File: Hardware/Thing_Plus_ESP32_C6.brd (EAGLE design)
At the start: 22.9 x 58.4 mm, 108 parts, among them J1 THING_PLUS_LOGICAL, J4 QWIIC_RIGHT_ANGLE, J5 MICRO-SDFRICTION, Q1 20V/4.2A/52mΩ/1.4W, U1 ESP32-C6-WROOM-1-NARROW, U2 RT9080-33GJ5, U3 MCP73831, U4 MAX17048

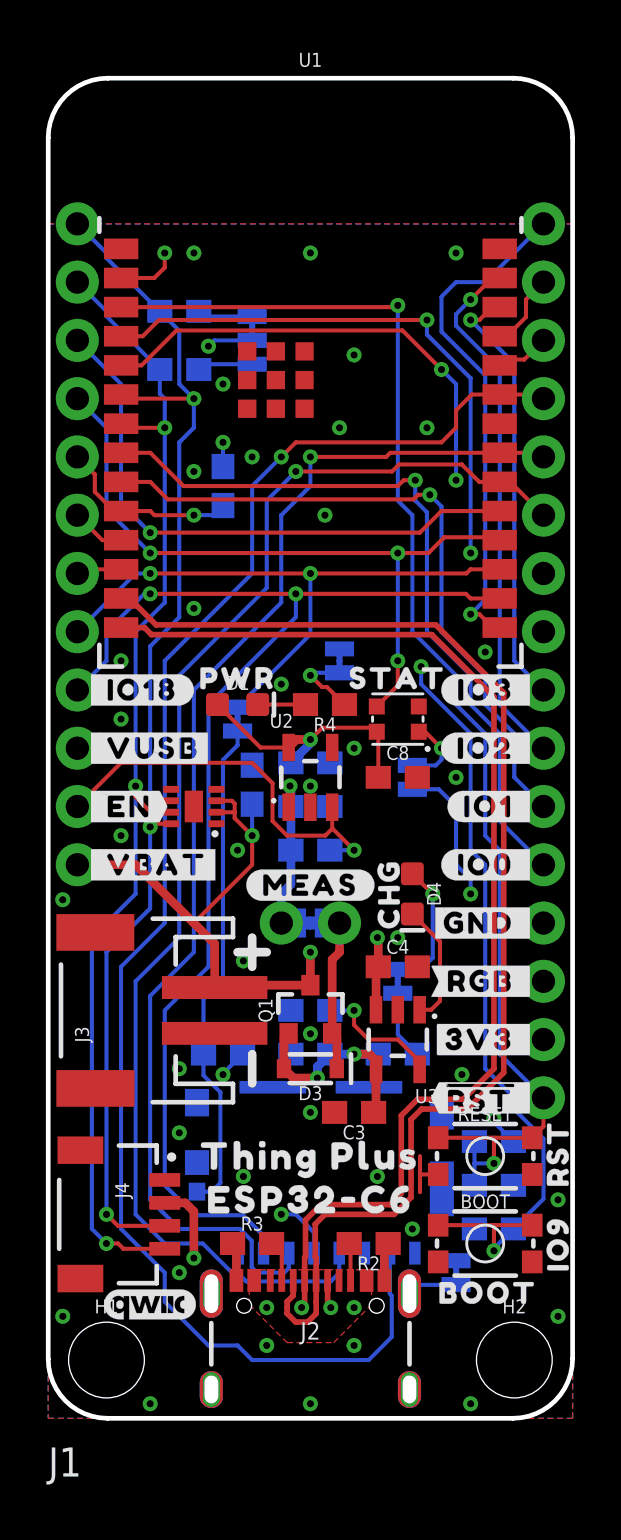
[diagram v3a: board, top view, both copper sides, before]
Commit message: Design review updates
Add fiducials
Add top mounting holes under ESP32-C6 antenna
Move OSHW logo and make bigger
Change RGB jumper to NO
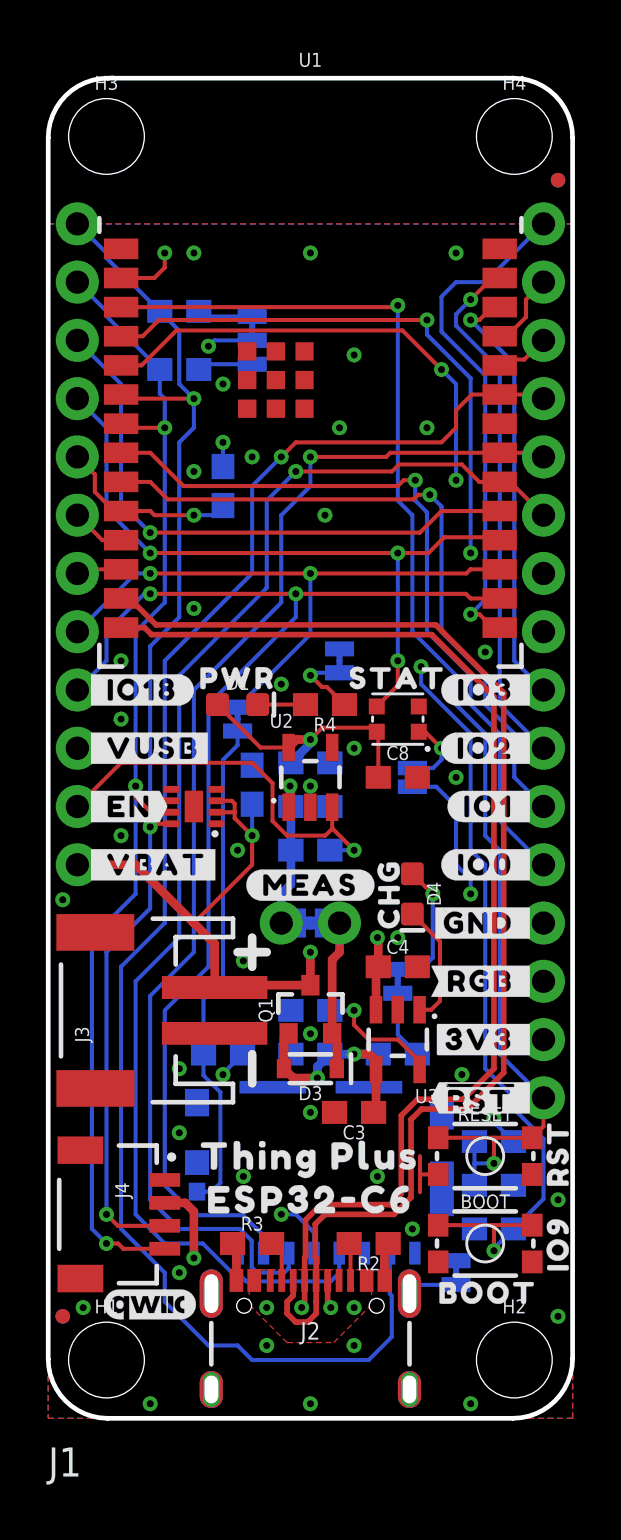
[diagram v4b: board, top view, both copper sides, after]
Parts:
- added FD1, FD2, FD3, FD4: FIDUCIALUFIDUCIAL, SparkFun-Aesthetics:FIDUCIAL-MICRO
- added H3, H4: STAND-OFF, SparkFun-Hardware:STAND-OFF
- LOGO3: value OSHW-LOGOS -> OSHW-LOGOM; device SparkFun-Aesthetics:OSHW-LOGO-S -> SparkFun-Aesthetics:OSHW-LOGO-M
- RGB: value JUMPER-SMT_2_NC_TRACE_SILK -> JUMPER-SMT_2_NO_SILK; device SparkFun-Jumpers:SMT-JUMPER_2_NC_TRACE_SILK -> SparkFun-Jumpers:SMT-JUMPER_2_NO_SILK
- moved LOGO3 20.9 mm to (5.08, 19.7)
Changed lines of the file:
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@@
 <element name="LOGO1" library="SparkFun-Aesthetics" package="SFE_LOGO_NAME_FLAME_.1" value="SFE_LOGO_NAME_FLAME.1_INCH" x="11.43" y="54.229" smashed="yes" rot="MR0"/>
 <element name="LOGO2" library="SparkFun-Aesthetics" package="QWIIC_4MM" value="QWIIC_LOGO_4MM" x="4.445" y="4.953" smashed="yes"/>
-<element name="LOGO3" library="SparkFun-Aesthetics" package="OSHW-LOGO-S" value="OSHW-LOGOS" x="10.16" y="40.005" smashed="yes" rot="MR0"/>
+<element name="LOGO3" library="SparkFun-Aesthetics" package="OSHW-LOGO-M" value="OSHW-LOGOM" x="5.08" y="19.685" smashed="yes" rot="MR0"/>
 <element name="R1" library="SparkFun-Resistors" package="0603" value="100k" x="7.62" y="40.64" smashed="yes" rot="MR90">
 <attribute name="NAME" x="8.182" y="40.64" size="0.6096" layer="26" font="vector" ratio="20" rot="MR90" align="bottom-center"/>
@@
 <element name="U$54" library="output" package="CHG0" value="" x="14.859" y="22.86" smashed="yes" rot="R90"/>
 <element name="U$55" library="output" package="STAT0" value="" x="15.24" y="32.258" smashed="yes"/>
-<element name="RGB" library="SparkFun-Jumpers" package="SMT-JUMPER_2_NC_TRACE_SILK" package3d_urn="urn:adsk.eagle:package:39281/1" value="JUMPER-SMT_2_NC_TRACE_SILK" x="15.875" y="27.94" smashed="yes" rot="MR90">
+<element name="RGB" library="SparkFun-Jumpers" package="SMT-JUMPER_2_NO_SILK" package3d_urn="urn:adsk.eagle:package:39279/1" value="JUMPER-SMT_2_NO_SILK" x="15.875" y="27.94" smashed="yes" rot="MR90">
 <attribute name="NAME" x="17.018" y="27.94" size="0.6096" layer="26" font="vector" ratio="20" rot="MR90" align="bottom-center"/>
 <attribute name="VALUE" x="14.732" y="27.94" size="0.6096" layer="28" font="vector" ratio="20" rot="MR90" align="top-center"/>
@@
 <element name="U$58" library="output" package="#RGB_#0" value="" x="21.336" y="19.05" smashed="yes"/>
 <element name="U$59" library="output" package="#_RGB#0" value="" x="21.336" y="19.05" smashed="yes" rot="MR0"/>
+<element name="H3" library="SparkFun-Hardware" package="STAND-OFF" value="STAND-OFF" x="2.54" y="55.88" smashed="yes">
+<attribute name="NAME" x="2.54" y="57.912" size="0.6096" layer="25" font="vector" ratio="20" align="bottom-center"/>
+<attribute name="VALUE" x="2.54" y="53.848" size="0.6096" layer="27" font="vector" ratio="20" align="top-center"/>
+</element>
+<element name="H4" library="SparkFun-Hardware" package="STAND-OFF" value="STAND-OFF" x="20.32" y="55.88" smashed="yes">
+<attribute name="NAME" x="20.32" y="57.912" size="0.6096" layer="25" font="vector" ratio="20" align="bottom-center"/>
+<attribute name="VALUE" x="20.32" y="53.848" size="0.6096" layer="27" font="vector" ratio="20" align="top-center"/>
+</element>
+<element name="FD1" library="SparkFun-Aesthetics" package="FIDUCIAL-MICRO" value="FIDUCIALUFIDUCIAL" x="22.225" y="53.975" smashed="yes"/>
+<element name="FD2" library="SparkFun-Aesthetics" package="FIDUCIAL-MICRO" value="FIDUCIALUFIDUCIAL" x="22.225" y="53.975" smashed="yes" rot="MR0"/>
+<element name="FD3" library="SparkFun-Aesthetics" package="FIDUCIAL-MICRO" value="FIDUCIALUFIDUCIAL" x="0.635" y="4.445" smashed="yes"/>
+<element name="FD4" library="SparkFun-Aesthetics" package="FIDUCIAL-MICRO" value="FIDUCIALUFIDUCIAL" x="0.635" y="4.445" smashed="yes" rot="MR0"/>
 </elements>
 <signals>
@@
 <via x="18.415" y="0.635" extent="1-16" drill="0.3048"/>
 <via x="4.445" y="0.635" extent="1-16" drill="0.3048"/>
-<via x="0.635" y="4.445" extent="1-16" drill="0.3048"/>
+<via x="1.524" y="4.826" extent="1-16" drill="0.3048"/>
 <via x="0.635" y="22.606" extent="1-16" drill="0.3048"/>
 <via x="8.255" y="24.765" extent="1-16" drill="0.3048"/>
@@
 <contactref element="J1" pad="26"/>
 <contactref element="RGB" pad="1"/>
-<wire x1="15.875" y1="27.4193" x2="17.0307" y2="27.4193" width="0.1778" layer="16"/>
-<wire x1="17.0307" y1="27.4193" x2="17.78" y2="26.67" width="0.1778" layer="16"/>
+<wire x1="15.875" y1="27.5336" x2="16.9164" y2="27.5336" width="0.1778" layer="16"/>
+<wire x1="16.9164" y1="27.5336" x2="17.78" y2="26.67" width="0.1778" layer="16"/>
 <wire x1="17.78" y1="26.67" x2="17.78" y2="24.13" width="0.1778" layer="16"/>
 <wire x1="17.78" y1="24.13" x2="18.415" y2="23.495" width="0.1778" layer="16"/>
@@
 <wire x1="16.425" y1="29.93" x2="17.145" y2="29.21" width="0.1778" layer="1"/>
 <via x="17.145" y="29.21" extent="1-16" drill="0.3048"/>
-<wire x1="17.145" y1="28.7147" x2="16.891" y2="28.4607" width="0.1778" layer="16"/>
-<wire x1="15.875" y1="28.4607" x2="16.891" y2="28.4607" width="0.1778" layer="16"/>
+<wire x1="17.145" y1="28.7147" x2="16.7767" y2="28.3464" width="0.1778" layer="16"/>
+<wire x1="15.875" y1="28.3464" x2="16.7767" y2="28.3464" width="0.1778" layer="16"/>
 <wire x1="17.145" y1="28.7147" x2="17.145" y2="29.21" width="0.1778" layer="16"/>
 </signal>

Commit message: Add power control to uSD card
Also add 10uF cap for uSD card
And add boot button text
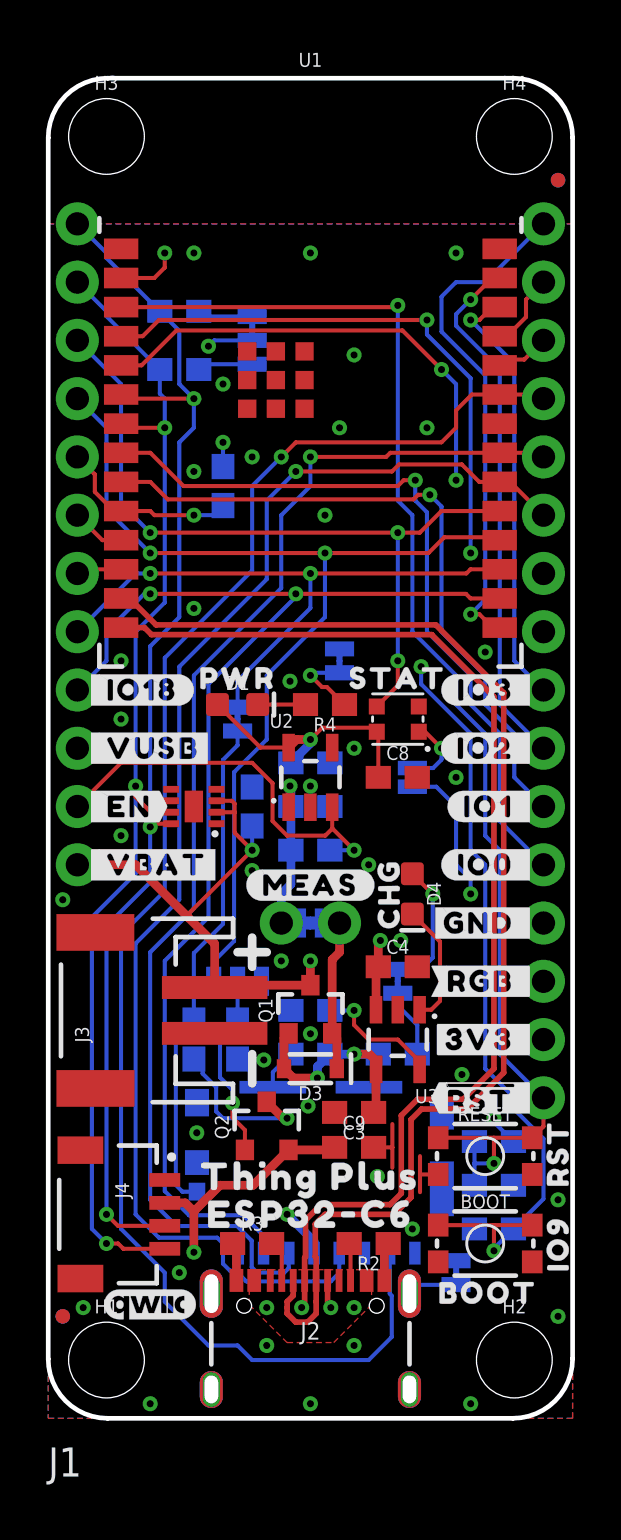
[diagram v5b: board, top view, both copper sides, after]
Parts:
- added C9: 10uF, SparkFun-Capacitors:0603
- added Q2: 20V/4.2A/52mΩ/1.4W, SparkFun-DiscreteSemi:SOT23-3
- added R13: 100k, SparkFun-Resistors:0603
- added SD_P: JUMPER-SMT_3_1-NC_TRACE_SILK, SparkFun-Jumpers:SMT-JUMPER_3_1-NC_TRACE_SILK
- added U$60: (no value), output:#SD_P#0
- moved LOGO3 7.24 mm to (3.17, 12.7)
- moved R5 1.42 mm to (6.35, 16.5), turned to 270 degrees
- moved C7 0.95 mm to (8.89, 26.7)
- moved U$45 0.89 mm to (11.4, 10.5)
- moved U$46 0.63 mm to (11.4, 8.89)
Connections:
- removed net IO20/STAT: D5.DI, J1.4, U1.18
- removed net IO21: J1.3, U1.19
- new net IO20/SD_POW: J1.4, SD_P.1, U1.18
- new net IO21/STAT: D5.DI, J1.3, U1.19
- new net N$15: J5.4, Q2.3, R5.2
- new net N$16: Q2.1, R13.1, SD_P.2
- net 3.3V: now also C9.1, Q2.2, R13.2; no longer J5.4, R5.2
- net GND: now also C9.2, SD_P.3
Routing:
- net IO20/SD_POW: track 0.00 -> 44.3 mm, vias 0 -> 2
- net IO21/STAT: track 0.00 -> 33.3 mm, vias 0 -> 3
- net IO20/STAT: track 30.7 -> 0.00 mm, vias 3 -> 0
- net IO21: track 25.3 -> 0.00 mm, vias 1 -> 0
- net N$15: track 0.00 -> 13.5 mm, vias 0 -> 2
- net N$16: track 0.00 -> 8.12 mm, vias 0 -> 1
- net GND: track 5.73 -> 10.2 mm, vias 40 -> 39
- net 3.3V: track 26.0 -> 30.4 mm, vias 8 -> 7
- net V_BATT: track 30.9 -> 30.2 mm
- net IO22/SCK: track 58.2 -> 58.7 mm
